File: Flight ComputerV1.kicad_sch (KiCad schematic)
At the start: 26 parts, among them J101 ICSP, J102 Screw_Terminal_01x02, J103 Conn_01x08, J104 Conn_01x07, J105 Micro_SD_Card, J106 Conn_02x10_Top_Bottom, SW101 1-1825910-8, U101 ATmega328PB-A, U102 LMT84DCK

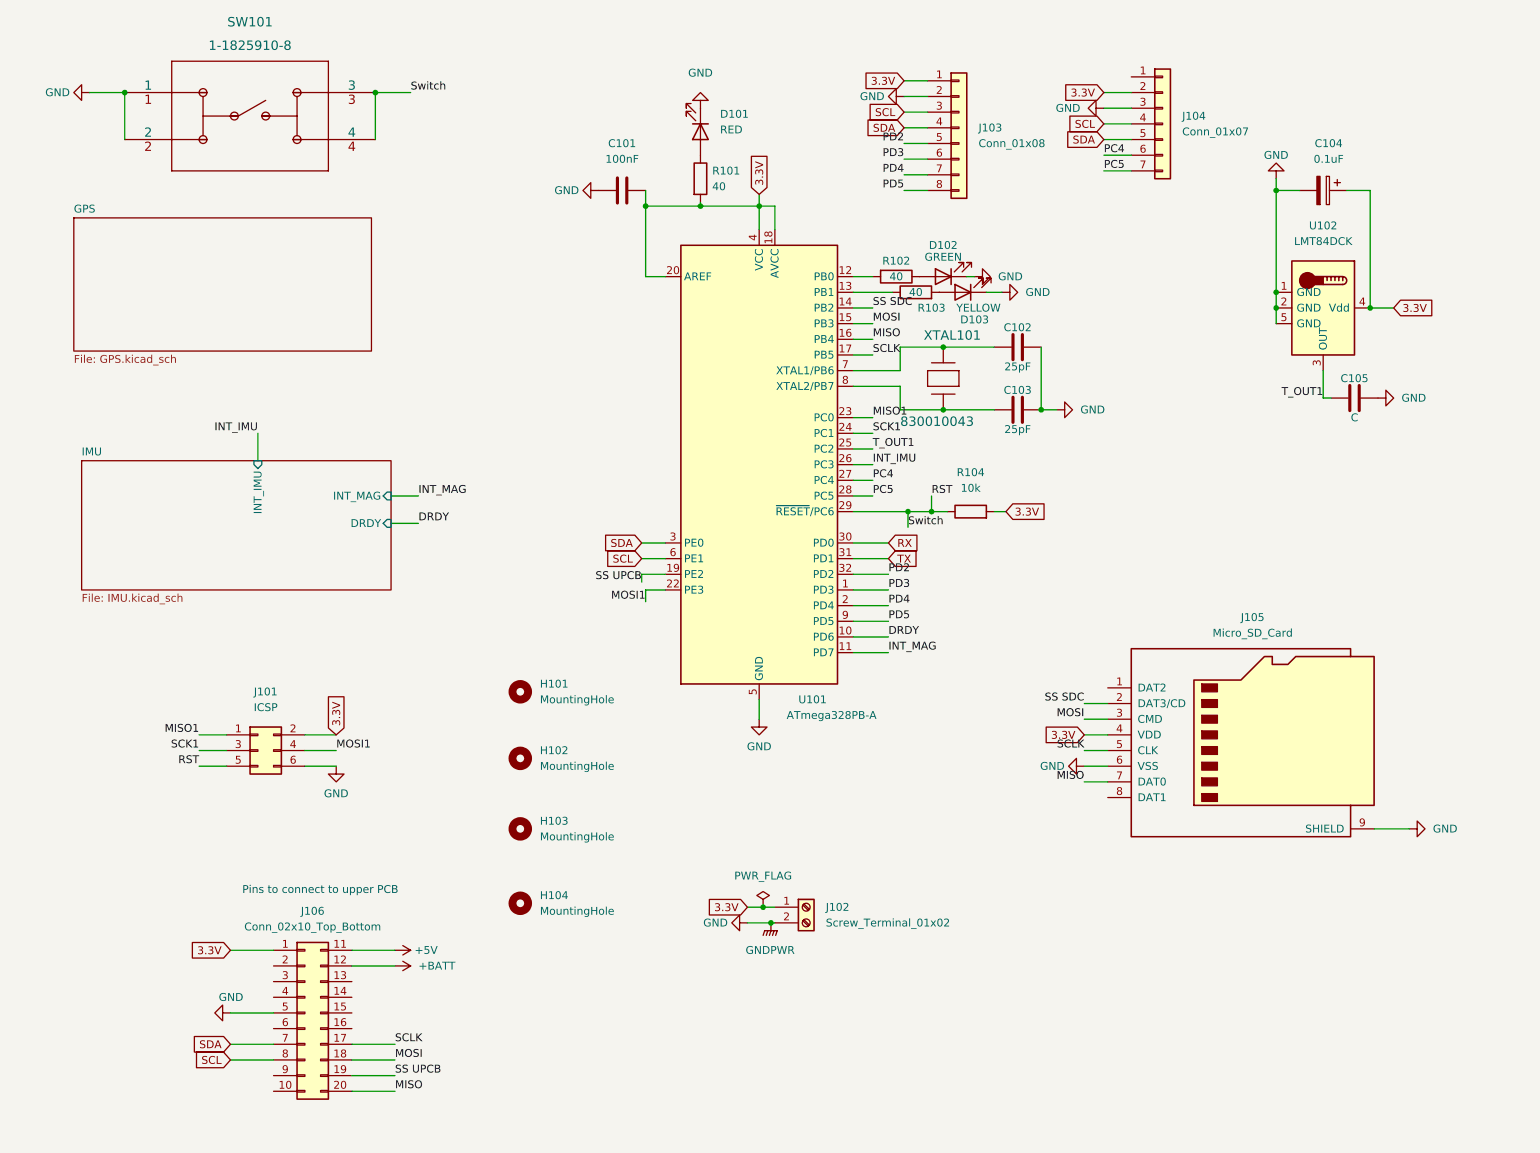
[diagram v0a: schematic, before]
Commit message: updates to schematics layout
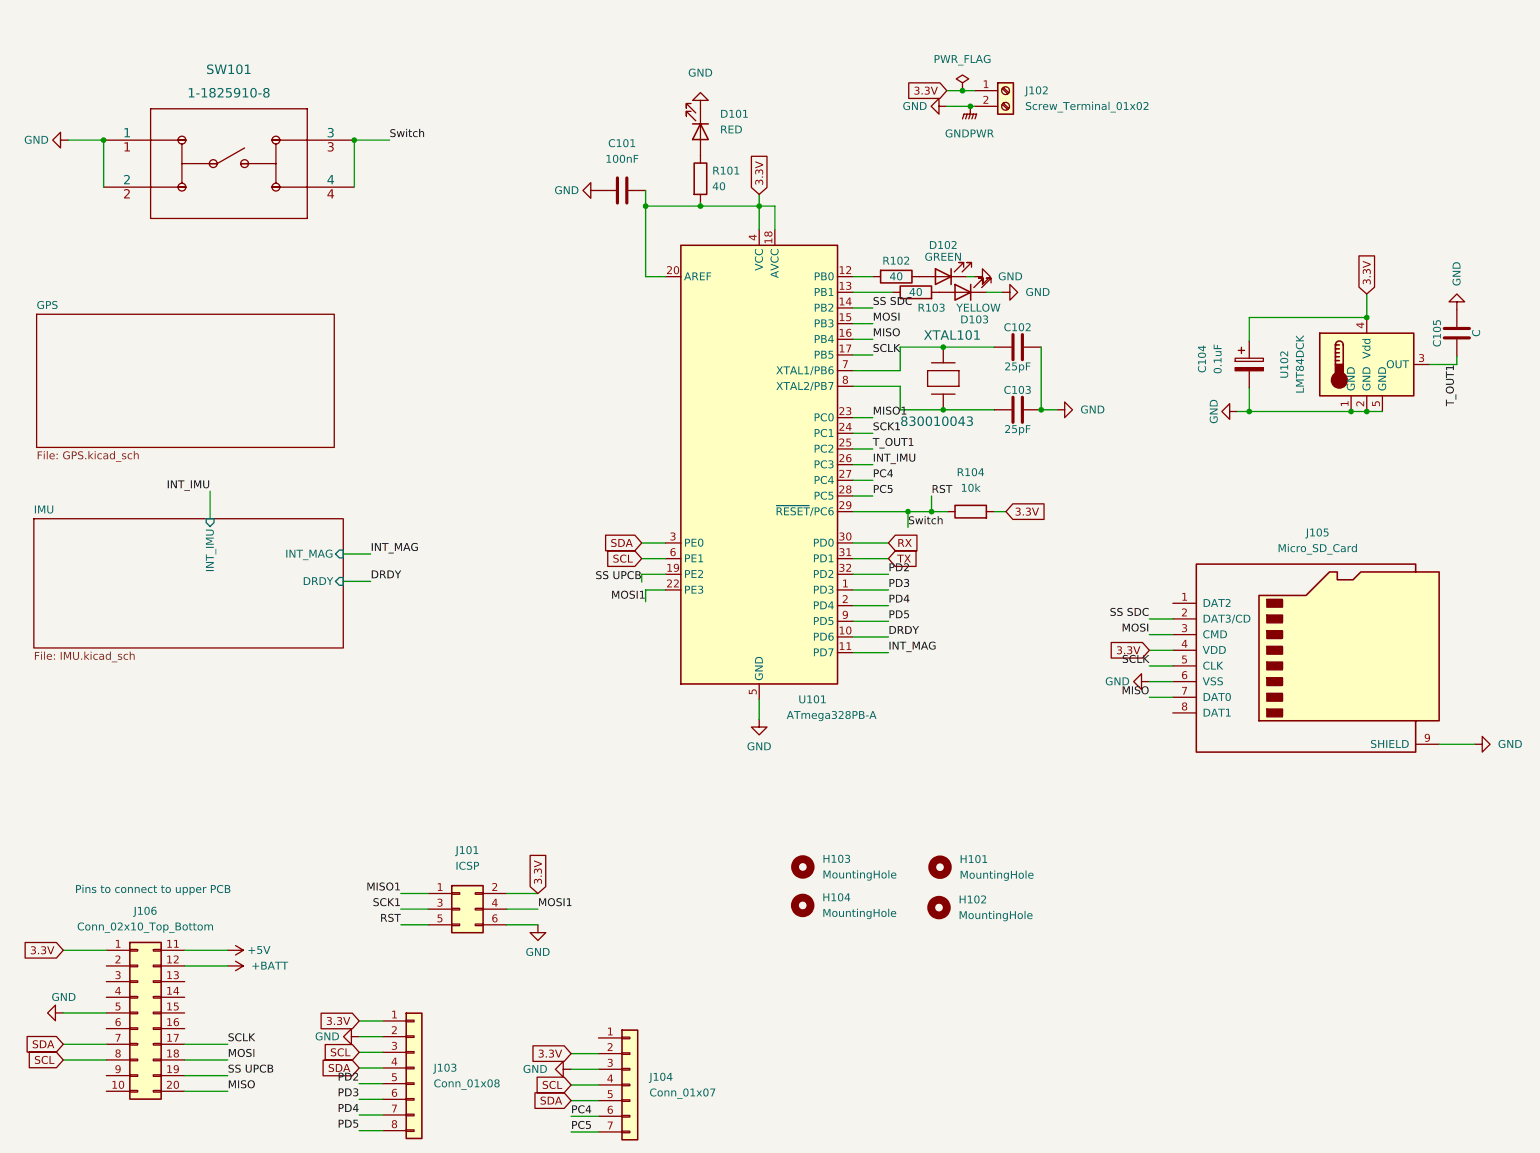
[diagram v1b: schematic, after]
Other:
- moved on the sheet: C104, C105, H101, H102, H103, H104, J101, J102, J103, J104, J105, J106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
